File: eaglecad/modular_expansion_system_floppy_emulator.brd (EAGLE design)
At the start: 80.6 x 101 mm, 36 parts, among them IC1 74LS00N, IC11 74LS20N, IC2 74LS373N, IC3 74LS30N, IC4 74LS244N, IC5 74S74N, IC6 74LS139N, IC7 74LS155N, J1-INTERRUPTS INTERRUPTS, J1_ADDRESS_CON J1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

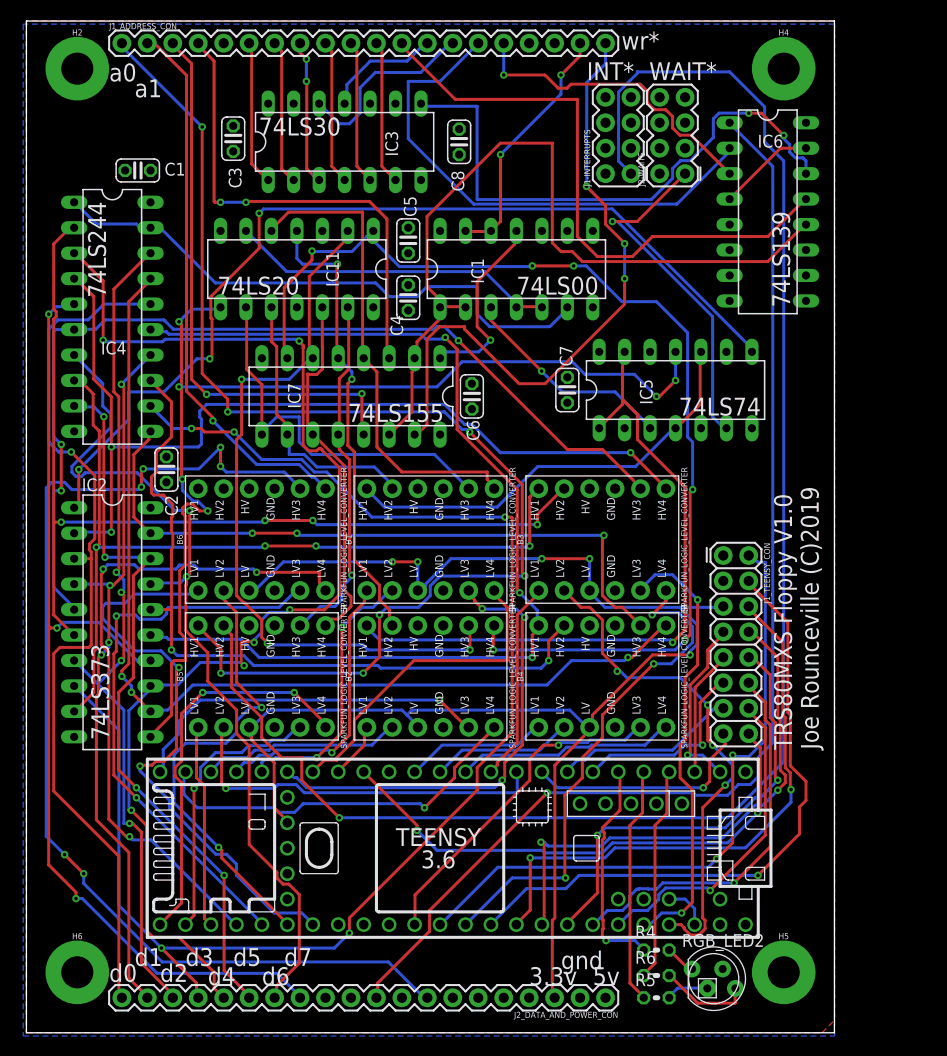
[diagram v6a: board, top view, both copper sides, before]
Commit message: Fixes for mount, stand alond joystick boards, level shifters Adafruit
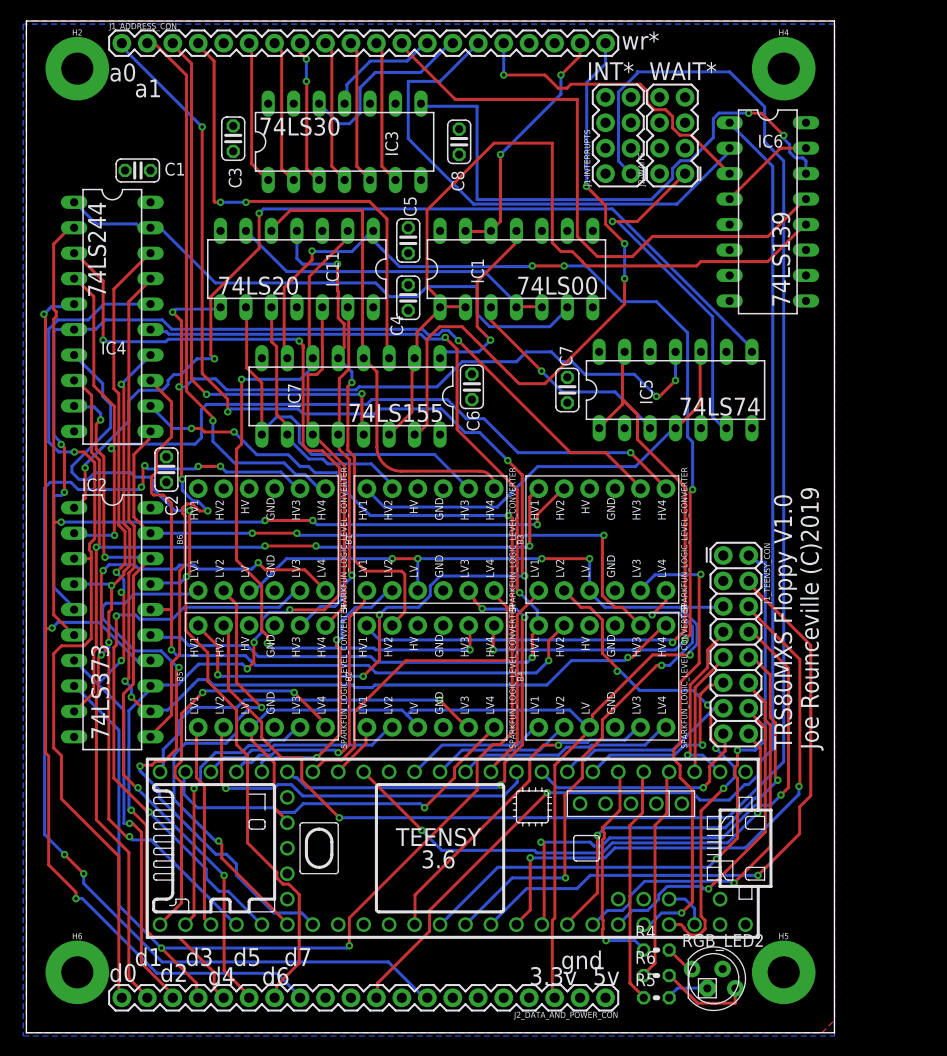
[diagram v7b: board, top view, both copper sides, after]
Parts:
- moved C6 0.95 mm to (44.8, 64.5)
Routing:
- net 37E8RD_: track 45.7 -> 49.4 mm
- net D1_LV: track 44.7 -> 47.2 mm
- net SYSRES*: track 111.6 -> 109.4 mm
- net 37EXWR: track 109.3 -> 111.4 mm
- net A0: track 125.9 -> 127.9 mm
- net D3: track 144.5 -> 146.2 mm
- net A1: track 54.9 -> 56.1 mm
- net D4_HV: track 100.6 -> 101.8 mm
- net D0_HV: track 93.4 -> 94.5 mm
- net 37E8WR_: track 36.2 -> 35.2 mm
- net VCC/2: track 153.5 -> 152.5 mm
- net D7: track 101.1 -> 102.1 mm
- net 37E4WR_LV_: track 27.2 -> 28.1 mm
- net 37E4WR_: track 27.5 -> 26.7 mm
- net D6: track 87.2 -> 87.9 mm
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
